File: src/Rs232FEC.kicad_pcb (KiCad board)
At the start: 2 copper layers, 24 x 27.9 mm, 26 parts, among them J1 B5B-XH-A, P1 105444-0001, Q1 DMP3099L-13, U1 FT232RL, U2 MAX232IDR

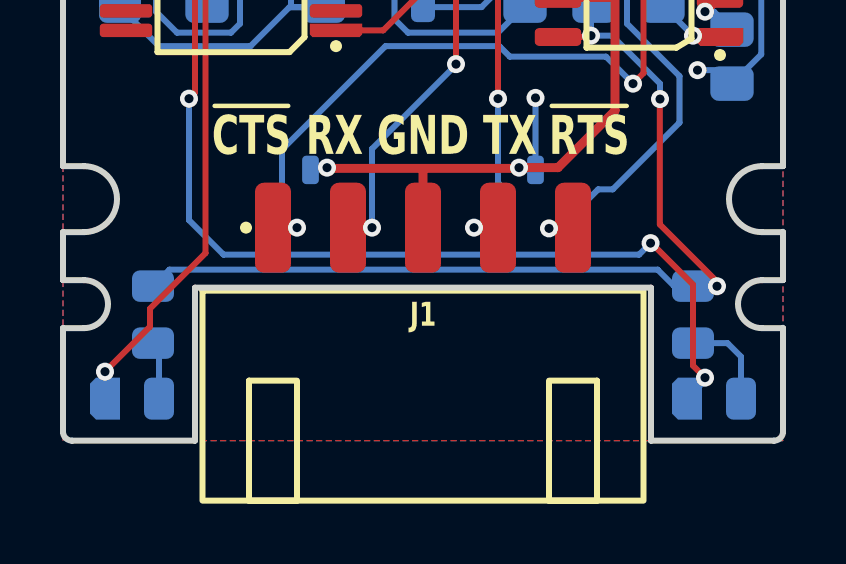
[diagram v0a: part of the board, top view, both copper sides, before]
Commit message: Updated connector designators
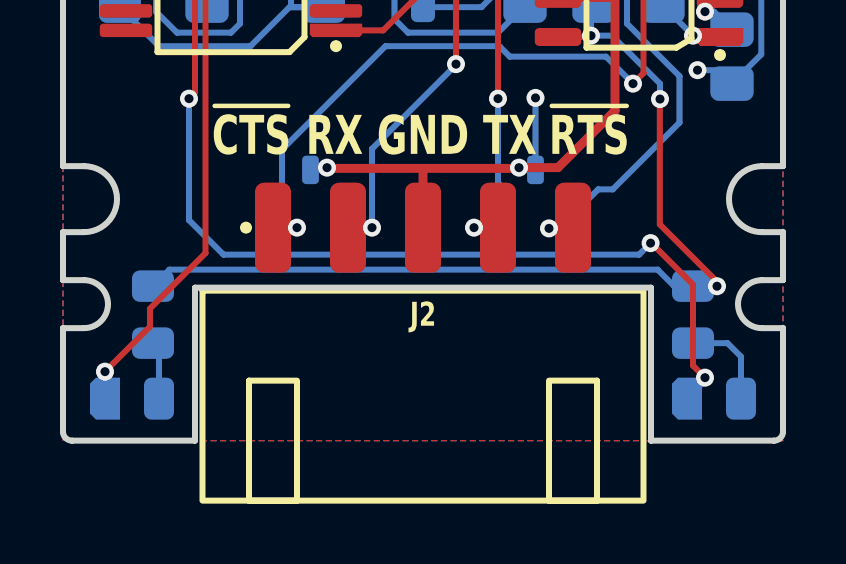
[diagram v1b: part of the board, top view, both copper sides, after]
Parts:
- renumbered P1 to J1, J1 to J2
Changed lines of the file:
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@@
     (descr "Molex 1054440001")
     (attr smd)
-    (fp_text reference "P1" (at 0 -1.7) (layer "F.SilkS") hide
+    (fp_text reference "J1" (at 0 -1.7) (layer "F.SilkS") hide
         (effects (font (size 0.8 0.6) (thickness 0.15)))
     )
@@
     (descr "JST B5B-XH-A [455-B5B-XH-A-ND]")
     (attr through_hole)
-    (fp_text reference "J1" (at 0 2.9) (layer "F.SilkS")
+    (fp_text reference "J2" (at 0 2.9) (layer "F.SilkS")
         (effects (font (size 0.8 0.6) (thickness 0.15) bold))
     )

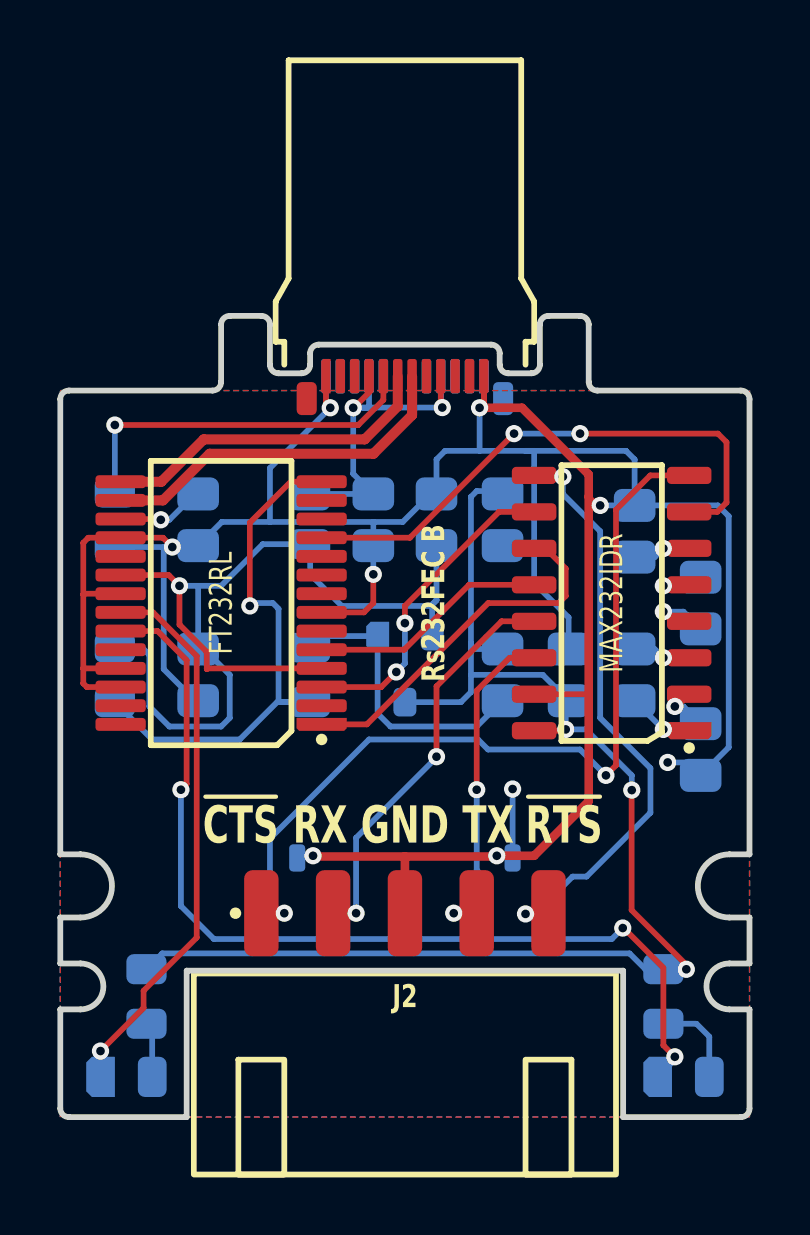
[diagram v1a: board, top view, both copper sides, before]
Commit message: Updated board RefDes
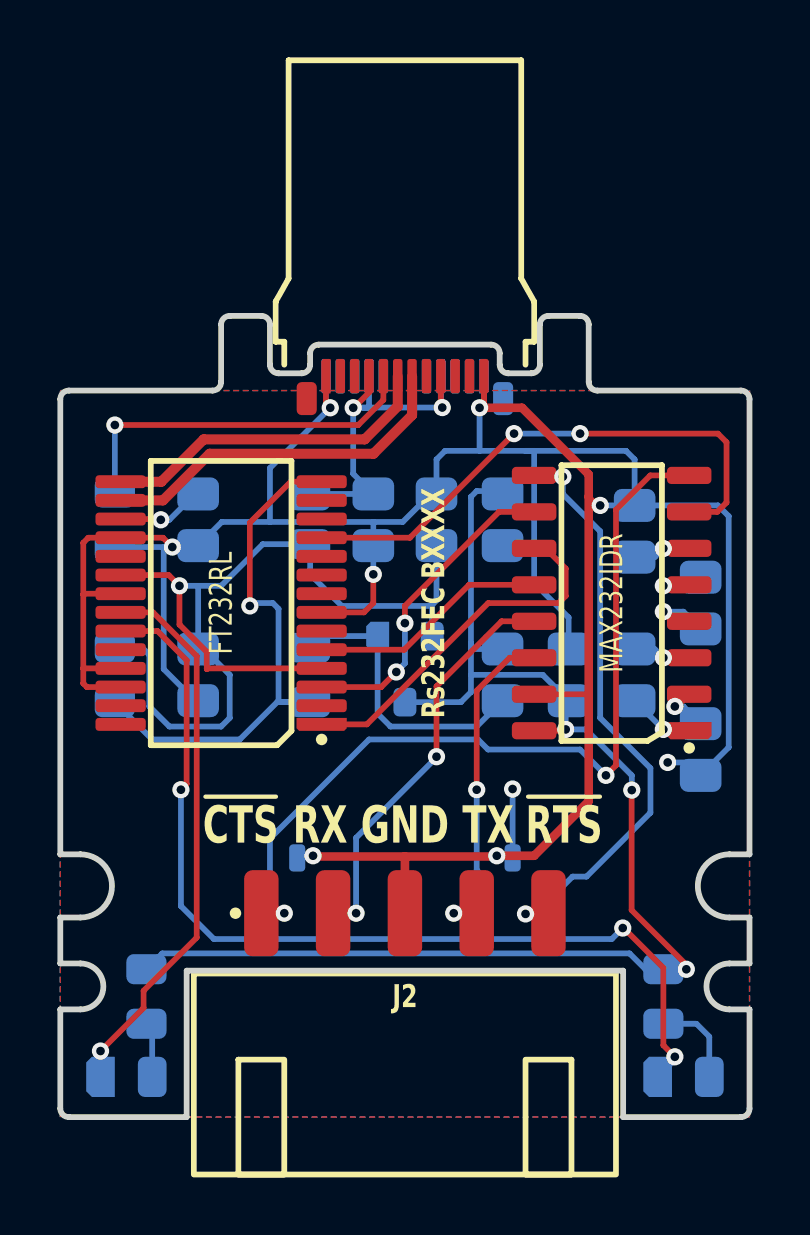
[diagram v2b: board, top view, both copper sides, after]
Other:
- board text added: "Rs232FEC BXXXX"
- board text removed: "Rs232FEC B"

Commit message: Cleaning up components
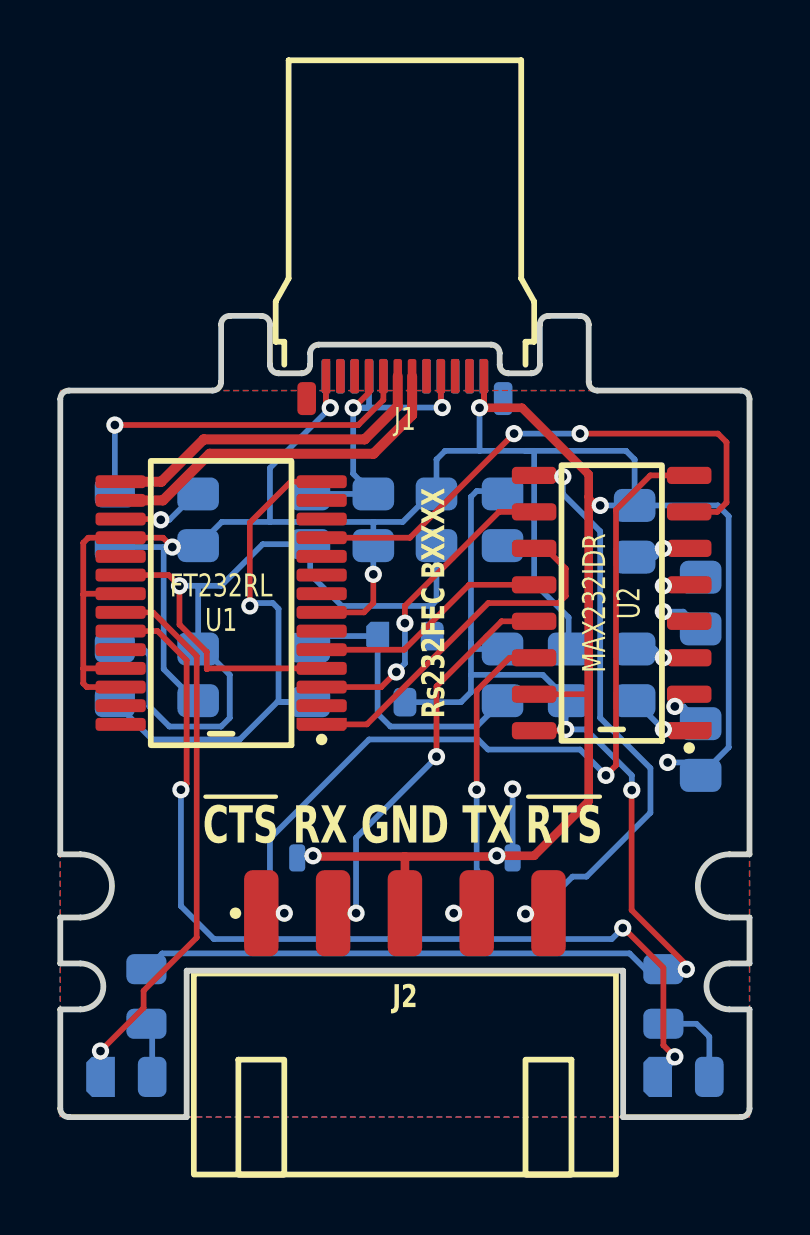
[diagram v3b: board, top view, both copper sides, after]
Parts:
- D1, D2: footprint Medo64:D TVS SM05T1G (SOT23-3) -> Medo64:D TVS 12V [PESD12VL2BT,215] (SOT23-3)
- J1: footprint Medo64:P USB C 3.2 Edge (24w) -> Medo64:J USB C 3.2 Edge (24w)
- J2: footprint Medo64:J JST XH Edge [UART] (5w) -> Medo64:J JST XH Edge [RS232] (5w)
- U1: footprint Medo64:U Transciever UART FT232RL (SSOP-28) -> Medo64:U Transceiver UART [FT232R] (SSOP-28)
- U2: footprint Medo64:U Transciever RS232 MAX232IDR (SOIC-16) -> Medo64:U Transceiver RS232 [MAX232IDR] (SOIC-16)
